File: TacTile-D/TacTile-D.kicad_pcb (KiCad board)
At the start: 2 copper layers, 59.9 x 59.9 mm, 19 parts, among them J1 Conn_01x06, J2 Conn_01x06, J3 Conn_01x06, J4 Conn_01x06, J5 Conn_01x04, J6 Conn_01x05, J7 Conn_01x02, J8 Conn_01x02, U1 74LVC2G08, U10 74LVC1G373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

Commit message: Made board D layout more efficient
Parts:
- moved U10 51.6 mm to (73.7, 37.7)
- moved U4 44.8 mm to (63.6, 75.3), turned to 90 degrees
- moved U3 41.3 mm to (28.6, 75.3), turned to 90 degrees
- moved U7 33.6 mm to (34.7, 51.2)
- moved U8 31.4 mm to (49.0, 37.7)
- moved U9 30.1 mm to (61.5, 37.7)
- moved U11 23.6 mm to (57.2, 51.2)
- moved U1 17.0 mm to (68.5, 51.2)
- moved U2 12.8 mm to (51.2, 67.7)
- moved U6 12.1 mm to (44.1, 35.2), turned to -90 degrees
- moved U5 5.51 mm to (46.0, 51.2)
- moved J4 1.55 mm to (50.0, 79.7)
- moved J2 1.35 mm to (50.0, 31.1)

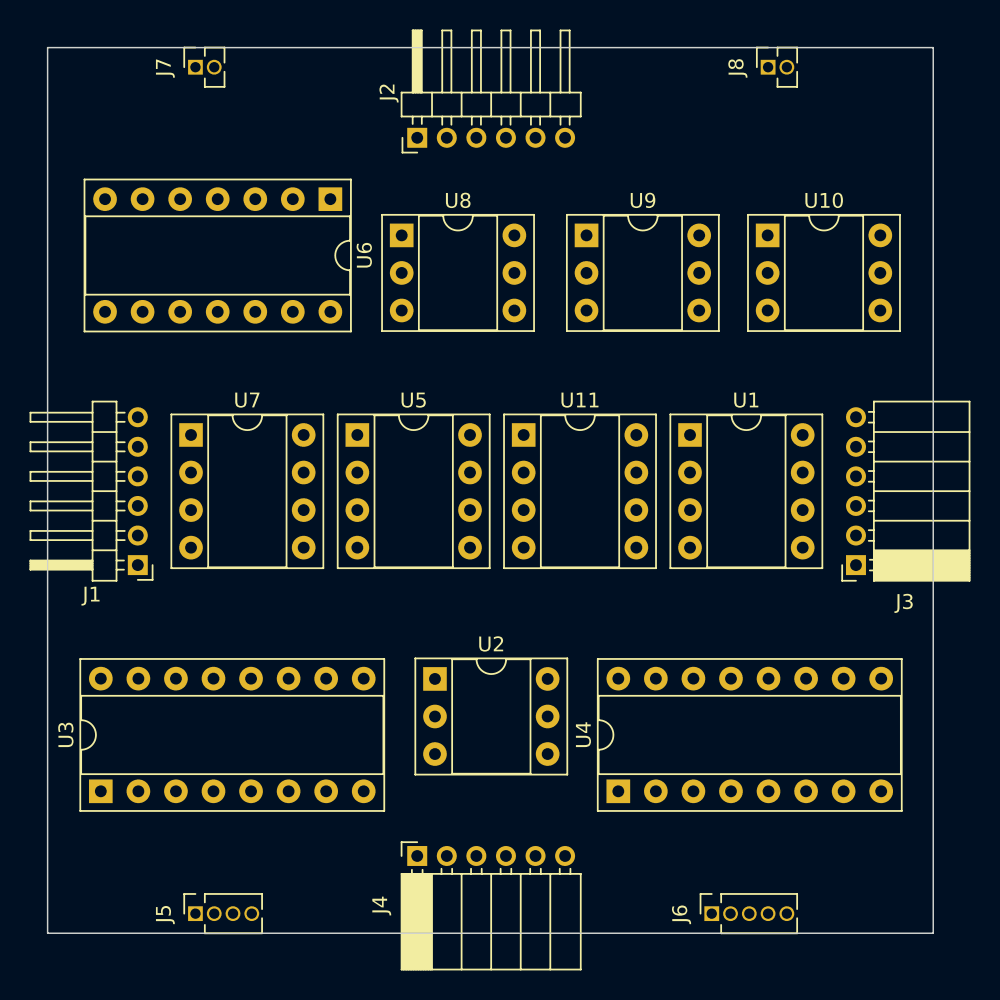
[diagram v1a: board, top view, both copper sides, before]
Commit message: Wired board D power traces
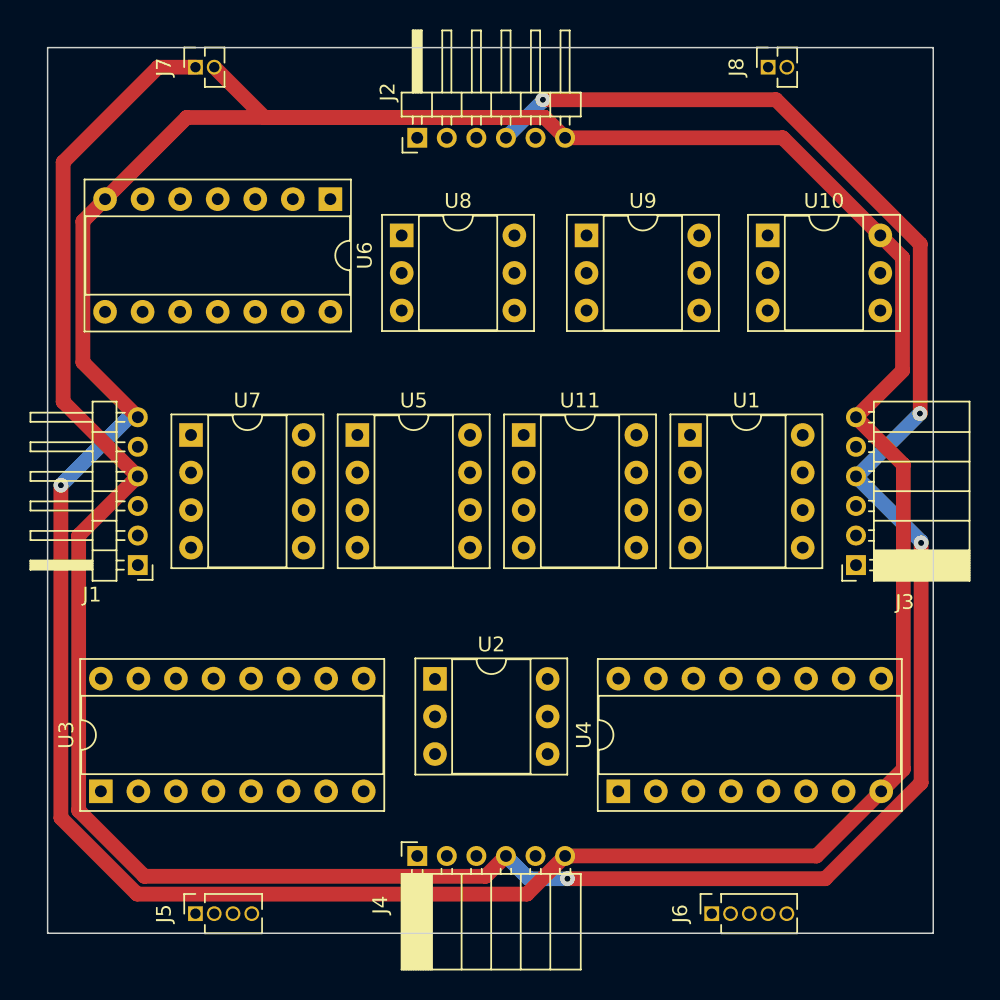
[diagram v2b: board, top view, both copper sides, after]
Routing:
- net GND: track 0.00 -> 230.3 mm, vias 0 -> 1
- net VIN: track 0.00 -> 195.2 mm, vias 0 -> 4
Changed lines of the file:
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@@
   )
   (setup
+    (stackup
+      (layer "F.SilkS" (type "Top Silk Screen"))
+      (layer "F.Paste" (type "Top Solder Paste"))
+      (layer "F.Mask" (type "Top Solder Mask") (thickness 0.01))
+      (layer "F.Cu" (type "copper") (thickness 0.035))
+      (layer "dielectric 1" (type "core") (thickness 1.51) (material "FR4") (epsilon_r 4.5) (loss_tangent 0.02))
+      (layer "B.Cu" (type "copper") (thickness 0.035))
+      (layer "B.Mask" (type "Bottom Solder Mask") (thickness 0.01))
+      (layer "B.Paste" (type "Bottom Solder Paste"))
+      (layer "B.SilkS" (type "Bottom Silk Screen"))
+      (copper_finish "None")
+      (dielectric_constraints no)
+    )
     (pad_to_mask_clearance 0)
     (pcbplotparams
@@
   (gr_rect (start 25 25) (end 84.9 84.9)
     (stroke (width 0.1) (type default)) (fill none) (layer "Edge.Cuts"))
+  (segment (start 74.266821 28.5255) (end 84.02 38.278679) (width 1) (layer "F.Cu") (net 4))
+  (segment (start 26.05 32.752944) (end 26.05 48.95) (width 1) (layer "F.Cu") (net 4))
+  (segment (start 84.02 49.73) (end 84 49.75) (width 1) (layer "F.Cu") (net 4))
+  (segment (start 27.1 58) (end 27.1 76.6) (width 1) (layer "F.Cu") (net 4))
+  (segment (start 27.1 76.6) (end 31.55 81.05) (width 1) (layer "F.Cu") (net 4))
+  (segment (start 54.625 81.05) (end 56 79.675) (width 1) (layer "F.Cu") (net 4))
+  (segment (start 77.590894 81.210427) (end 60.160924 81.210427) (width 1) (layer "F.Cu") (net 4))
+  (segment (start 84.02 38.278679) (end 84.02 49.73) (width 1) (layer "F.Cu") (net 4))
+  (segment (start 35 26.325) (end 32.477944 26.325) (width 1) (layer "F.Cu") (net 4))
+  (segment (start 32.477944 26.325) (end 26.05 32.752944) (width 1) (layer "F.Cu") (net 4))
+  (segment (start 58.5 28.5255) (end 74.266821 28.5255) (width 1) (layer "F.Cu") (net 4))
+  (segment (start 26.05 48.95) (end 31.1 54) (width 1) (layer "F.Cu") (net 4))
+  (segment (start 84.08 74.721321) (end 77.590894 81.210427) (width 1) (layer "F.Cu") (net 4))
+  (segment (start 31.1 54) (end 27.1 58) (width 1) (layer "F.Cu") (net 4))
+  (segment (start 84.08 58.5) (end 84.08 74.721321) (width 1) (layer "F.Cu") (net 4))
+  (segment (start 31.55 81.05) (end 54.625 81.05) (width 1) (layer "F.Cu") (net 4))
+  (via (at 58.5 28.5255) (size 1) (drill 0.4) (layers "F.Cu" "B.Cu") (net 4))
+  (via (at 84 49.75) (size 1) (drill 0.4) (layers "F.Cu" "B.Cu") (net 4))
+  (via (at 60.160924 81.210427) (size 1) (drill 0.4) (layers "F.Cu" "B.Cu") (net 4))
+  (via (at 84.08 58.5) (size 1) (drill 0.4) (layers "F.Cu" "B.Cu") (net 4))
+  (segment (start 56 79.675) (end 57.535427 81.210427) (width 1) (layer "B.Cu") (net 4))
+  (segment (start 79.675 54) (end 79.75 54) (width 1) (layer "B.Cu") (net 4))
+  (segment (start 84.08 58.405) (end 79.675 54) (width 1) (layer "B.Cu") (net 4))
+  (segment (start 84.08 58.5) (end 84.08 58.405) (width 1) (layer "B.Cu") (net 4))
+  (segment (start 58.5 28.5255) (end 58.5 28.6) (width 1) (layer "B.Cu") (net 4))
+  (segment (start 79.75 54) (end 84 49.75) (width 1) (layer "B.Cu") (net 4))
+  (segment (start 57.535427 81.210427) (end 60.160924 81.210427) (width 1) (layer "B.Cu") (net 4))
+  (segment (start 58.5 28.6) (end 56 31.1) (width 1) (layer "B.Cu") (net 4))
+  (segment (start 31.052944 82.25) (end 57.425 82.25) (width 1) (layer "F.Cu") (net 6))
+  (segment (start 27.385 36.75) (end 27.385 46.285) (width 1) (layer "F.Cu") (net 6))
+  (segment (start 74.72 31.1) (end 60 31.1) (width 1) (layer "F.Cu") (net 6))
+  (segment (start 77.005 79.675) (end 81.38 75.3) (width 1) (layer "F.Cu") (net 6))
+  (segment (start 58.625 29.725) (end 34.41 29.725) (width 1) (layer "F.Cu") (net 6))
+  (segment (start 82.88 73.8) (end 82.88 53.205) (width 1) (layer "F.Cu") (net 6))
+  (segment (start 82.82 39.2) (end 81.32 37.7) (width 1) (layer "F.Cu") (net 6))
+  (segment (start 27.385 46.285) (end 31.1 50) (width 1) (layer "F.Cu") (net 6))
+  (segment (start 82.88 53.205) (end 79.675 50) (width 1) (layer "F.Cu") (net 6))
+  (segment (start 79.675 50) (end 82.82 46.855) (width 1) (layer "F.Cu") (net 6))
+  (segment (start 60 31.1) (end 58.625 29.725) (width 1) (layer "F.Cu") (net 6))
+  (segment (start 81.38 75.3) (end 82.88 73.8) (width 1) (layer "F.Cu") (net 6))
+  (segment (start 25.9 54.6) (end 25.9 77.097056) (width 1) (layer "F.Cu") (net 6))
+  (segment (start 34.41 29.725) (end 28.885 35.25) (width 1) (layer "F.Cu") (net 6))
+  (segment (start 82.82 46.855) (end 82.82 39.2) (width 1) (layer "F.Cu") (net 6))
+  (segment (start 81.32 37.7) (end 74.72 31.1) (width 1) (layer "F.Cu") (net 6))
+  (segment (start 36.27 26.325) (end 39.67 29.725) (width 1) (layer "F.Cu") (net 6))
+  (segment (start 28.885 35.25) (end 27.385 36.75) (width 1) (layer "F.Cu") (net 6))
+  (segment (start 25.9 77.097056) (end 31.052944 82.25) (width 1) (layer "F.Cu") (net 6))
+  (segment (start 39.67 29.725) (end 58.625 29.725) (width 1) (layer "F.Cu") (net 6))
+  (segment (start 57.425 82.25) (end 60 79.675) (width 1) (layer "F.Cu") (net 6))
+  (segment (start 60 79.675) (end 77.005 79.675) (width 1) (layer "F.Cu") (net 6))
+  (via (at 25.9 54.6) (size 1) (drill 0.4) (layers "F.Cu" "B.Cu") (net 6))
+  (segment (start 25.9 54.6) (end 30.5 50) (width 1) (layer "B.Cu") (net 6))
+  (segment (start 30.5 50) (end 31.1 50) (width 1) (layer "B.Cu") (net 6))
 )

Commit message: Began routing Board D
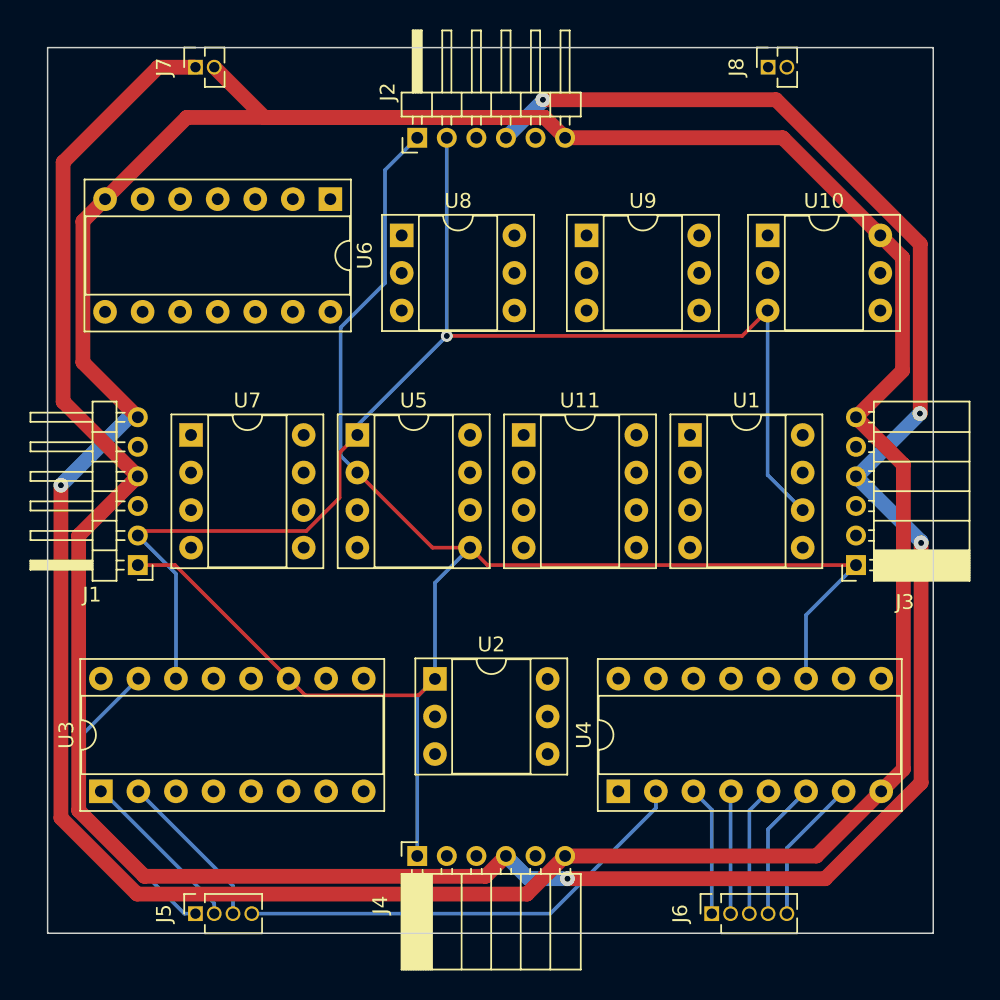
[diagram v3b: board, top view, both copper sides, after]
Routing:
- net CLK: track 0.00 -> 117.2 mm
- net MOSI: track 0.00 -> 90.3 mm, vias 0 -> 1
- net LS3: track 0.00 -> 31.4 mm
- net LS0: track 0.00 -> 21.0 mm
- net LS1: track 0.00 -> 11.5 mm
- net LS2: track 0.00 -> 10.9 mm
- net LS8: track 0.00 -> 9.87 mm
- net LS7: track 0.00 -> 9.34 mm
- net LS6: track 0.00 -> 8.81 mm
- net LS4: track 0.00 -> 8.79 mm
- net LS5: track 0.00 -> 8.29 mm
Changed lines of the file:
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@@
   (gr_rect (start 25 25) (end 84.9 84.9)
     (stroke (width 0.1) (type default)) (fill none) (layer "Edge.Cuts"))
+  (segment (start 33.62 60) (end 31.1 60) (width 0.25) (layer "F.Cu") (net 1))
+  (segment (start 53.57 58.82) (end 51.03 58.82) (width 0.25) (layer "F.Cu") (net 1))
+  (segment (start 42.425 68.805) (end 41.3 67.68) (width 0.25) (layer "F.Cu") (net 1))
+  (segment (start 53.57 58.82) (end 54.75 60) (width 0.25) (layer "F.Cu") (net 1))
+  (segment (start 51.2 67.7) (end 50.095 68.805) (width 0.25) (layer "F.Cu") (net 1))
+  (segment (start 51.03 58.82) (end 45.95 53.74) (width 0.25) (layer "F.Cu") (net 1))
+  (segment (start 54.75 60) (end 79.675 60) (width 0.25) (layer "F.Cu") (net 1))
+  (segment (start 41.3 67.68) (end 33.62 60) (width 0.25) (layer "F.Cu") (net 1))
+  (segment (start 50.095 68.805) (end 42.425 68.805) (width 0.25) (layer "F.Cu") (net 1))
+  (segment (start 44.825 52.615) (end 44.825 43.925) (width 0.25) (layer "B.Cu") (net 1))
+  (segment (start 76.3 63.375) (end 79.675 60) (width 0.25) (layer "B.Cu") (net 1))
+  (segment (start 50 68.9) (end 51.2 67.7) (width 0.25) (layer "B.Cu") (net 1))
+  (segment (start 51.2 61.19) (end 53.57 58.82) (width 0.25) (layer "B.Cu") (net 1))
+  (segment (start 50 79.675) (end 50 68.9) (width 0.25) (layer "B.Cu") (net 1))
+  (segment (start 44.825 43.925) (end 47.825 40.925) (width 0.25) (layer "B.Cu") (net 1))
+  (segment (start 47.825 40.925) (end 47.825 33.275) (width 0.25) (layer "B.Cu") (net 1))
+  (segment (start 51.2 67.7) (end 51.2 61.19) (width 0.25) (layer "B.Cu") (net 1))
+  (segment (start 76.3 67.68) (end 76.3 63.375) (width 0.25) (layer "B.Cu") (net 1))
+  (segment (start 47.825 33.275) (end 50 31.1) (width 0.25) (layer "B.Cu") (net 1))
+  (segment (start 45.95 53.74) (end 44.825 52.615) (width 0.25) (layer "B.Cu") (net 1))
+  (segment (start 45.95 50.55) (end 45.95 51.2) (width 0.25) (layer "F.Cu") (net 2))
+  (segment (start 44.75 55.440991) (end 44.75 52.4) (width 0.25) (layer "F.Cu") (net 2))
+  (segment (start 31.1 58) (end 31.405 57.695) (width 0.25) (layer "F.Cu") (net 2))
+  (segment (start 73.7 42.78) (end 71.98 44.5) (width 0.25) (layer "F.Cu") (net 2))
+  (segment (start 42.495991 57.695) (end 44.75 55.440991) (width 0.25) (layer "F.Cu") (net 2))
+  (segment (start 31.405 57.695) (end 42.495991 57.695) (width 0.25) (layer "F.Cu") (net 2))
+  (segment (start 44.75 52.4) (end 45.95 51.2) (width 0.25) (layer "F.Cu") (net 2))
+  (segment (start 71.98 44.5) (end 52 44.5) (width 0.25) (layer "F.Cu") (net 2))
+  (via (at 52 44.5) (size 0.8) (drill 0.4) (layers "F.Cu" "B.Cu") (net 2))
+  (segment (start 33.68 67.68) (end 33.68 60.58) (width 0.25) (layer "B.Cu") (net 2))
+  (segment (start 52 31.1) (end 52 44.5) (width 0.25) (layer "B.Cu") (net 2))
+  (segment (start 76.07 56.28) (end 73.7 53.91) (width 0.25) (layer "B.Cu") (net 2))
+  (segment (start 45.95 51.2) (end 45.95 50.55) (width 0.25) (layer "B.Cu") (net 2))
+  (segment (start 73.7 53.91) (end 73.7 42.78) (width 0.25) (layer "B.Cu") (net 2))
+  (segment (start 33.68 60.58) (end 31.1 58) (width 0.25) (layer "B.Cu") (net 2))
+  (segment (start 45.95 50.55) (end 52 44.5) (width 0.25) (layer "B.Cu") (net 2))
   (segment (start 74.266821 28.5255) (end 84.02 38.278679) (width 1) (layer "F.Cu") (net 4))
   (segment (start 26.05 32.752944) (end 26.05 48.95) (width 1) (layer "F.Cu") (net 4))
@@
   (segment (start 25.9 54.6) (end 30.5 50) (width 1) (layer "B.Cu") (net 6))
   (segment (start 30.5 50) (end 31.1 50) (width 1) (layer "B.Cu") (net 6))
+  (segment (start 34.25 83.575) (end 27.475 76.8) (width 0.25) (layer "B.Cu") (net 9))
+  (segment (start 35 83.575) (end 34.25 83.575) (width 0.25) (layer "B.Cu") (net 9))
+  (segment (start 27.475 71.345) (end 31.14 67.68) (width 0.25) (layer "B.Cu") (net 9))
+  (segment (start 27.475 76.8) (end 27.475 71.345) (width 0.25) (layer "B.Cu") (net 9))
+  (segment (start 28.702106 75.3) (end 28.6 75.3) (width 0.25) (layer "B.Cu") (net 10))
+  (segment (start 36.27 82.867894) (end 28.702106 75.3) (width 0.25) (layer "B.Cu") (net 10))
+  (segment (start 36.27 83.575) (end 36.27 82.867894) (width 0.25) (layer "B.Cu") (net 10))
+  (segment (start 37.54 83.575) (end 37.54 81.7) (width 0.25) (layer "B.Cu") (net 11))
+  (segment (start 37.54 81.7) (end 31.14 75.3) (width 0.25) (layer "B.Cu") (net 11))
+  (segment (start 58.99637 83.575) (end 38.81 83.575) (width 0.25) (layer "B.Cu") (net 12))
+  (segment (start 66.14 76.43137) (end 58.99637 83.575) (width 0.25) (layer "B.Cu") (net 12))
+  (segment (start 66.14 75.3) (end 66.14 76.43137) (width 0.25) (layer "B.Cu") (net 12))
+  (segment (start 69.92 76.54) (end 68.68 75.3) (width 0.25) (layer "B.Cu") (net 13))
+  (segment (start 69.92 83.575) (end 69.92 76.54) (width 0.25) (layer "B.Cu") (net 13))
+  (segment (start 71.19 75.33) (end 71.22 75.3) (width 0.25) (layer "B.Cu") (net 14))
+  (segment (start 71.19 83.575) (end 71.19 75.33) (width 0.25) (layer "B.Cu") (net 14))
+  (segment (start 72.46 76.6) (end 73.76 75.3) (width 0.25) (layer "B.Cu") (net 15))
+  (segment (start 72.46 83.575) (end 72.46 76.6) (width 0.25) (layer "B.Cu") (net 15))
+  (segment (start 73.73 83.575) (end 73.73 77.87) (width 0.25) (layer "B.Cu") (net 16))
+  (segment (start 73.73 77.87) (end 76.3 75.3) (width 0.25) (layer "B.Cu") (net 16))
+  (segment (start 75 83.575) (end 75 79.14) (width 0.25) (layer "B.Cu") (net 17))
+  (segment (start 75 79.14) (end 78.84 75.3) (width 0.25) (layer "B.Cu") (net 17))
 )

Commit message: Finished board D routing
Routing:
- net GND: track 230.3 -> 0.00 mm, vias 1 -> 0
- net VCC: track 0.00 -> 178.7 mm, vias 0 -> 1
- net SS: track 0.00 -> 101.6 mm, vias 0 -> 2
- net Net-(U10-LE): track 0.00 -> 67.6 mm, vias 0 -> 2
- net SEN: track 0.00 -> 66.7 mm
- net Net-(U6A-~{Q}): track 0.00 -> 63.9 mm, vias 0 -> 2
- net LEN: track 0.00 -> 53.2 mm
- net Net-(U3-RCLK): track 0.00 -> 51.5 mm, vias 0 -> 1
- net MISO0: track 0.00 -> 44.5 mm, vias 0 -> 2
- net MISO1: track 0.00 -> 40.4 mm, vias 0 -> 2
- net Net-(U11-Q): track 0.00 -> 37.1 mm, vias 0 -> 2
- net Net-(U6A-C): track 0.00 -> 35.3 mm, vias 0 -> 1
- net Net-(U10-Q): track 0.00 -> 33.5 mm
- net Net-(U6A-D): track 0.00 -> 29.4 mm
- net Net-(U11-C): track 0.00 -> 25.2 mm, vias 0 -> 1
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- added copper zone on B.Cu, net GND
- added copper zone on F.Cu, net GND
